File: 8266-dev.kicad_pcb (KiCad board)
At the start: 2 copper layers, 1 part, among them U1 ESP8266-12F_ESP-12F

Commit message: updated to v1
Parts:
- added BT1: Battery, Battery:BatteryHolder_MPD_BC2003_1x2032, F.Cu at (-32.3, 35.3)
- added C1: 10uF, Capacitor_SMD:C_1206_3216Metric, F.Cu at (-20.6, -21.4)
- added C2: 100nF, Capacitor_SMD:C_1206_3216Metric, F.Cu at (-15.3, -21.3)
- added G*** (x6): LOGO, LOGO, F.Cu at (0.00, 0.00)
- added J1: Conn_01x05_Female, digikey-kicad-library:PinHeader_1x5_P2.5mm_Drill1.1mm, F.Cu at (32.0, 35.0)
- added J2: Conn_01x05_Female, digikey-kicad-library:PinHeader_1x5_P2.5mm_Drill1.1mm, F.Cu at (-38.1, -34.8)
- added J3: Conn_01x06_Female, Connector_PinHeader_2.54mm:PinHeader_1x06_P2.54mm_Vertical, F.Cu at (19.8, 35.1)
- added J4: Conn_01x03_Female, digikey-kicad-library:PinHeader_1x3_P2.54_Drill1.1mm, F.Cu at (41.4, -32.7)
- added R1: 10K, Resistor_SMD:R_1206_3216Metric, F.Cu at (-19.9, -36.6)
- added R2: 10K, Resistor_SMD:R_1206_3216Metric, F.Cu at (-20.0, -32.7)
- added R3: 10K, Resistor_SMD:R_1206_3216Metric, F.Cu at (28.4, -40.5)
- added R4: 10K, Resistor_SMD:R_1206_3216Metric, F.Cu at (17.8, -24.4)
- added S1: 430152070826, digikey-kicad-library:Switch_Tactile_SMD_6x6mm, F.Cu at (31.3, -28.6)
- U1: moved to F.Cu
- moved U1 177.7 mm to (-0.53, -29.7), turned to 0 degrees
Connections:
- U1 pad 10: Net-(U1-Pad10) -> /MISO
- U1 pad 11: Net-(U1-Pad11) -> /IO9
- U1 pad 12: Net-(U1-Pad12) -> /IO10
- U1 pad 13: Net-(U1-Pad13) -> /MOSI
- U1 pad 14: Net-(U1-Pad14) -> /SCLK
- U1 pad 15: Net-(U1-Pad15) -> GND
- U1 pad 17: Net-(U1-Pad17) -> /IO2
- U1 pad 19: Net-(U1-Pad19) -> /IO4
- U1 pad 2: Net-(U1-Pad2) -> /ADC
- U1 pad 20: Net-(U1-Pad20) -> /IO5
- U1 pad 21: Net-(U1-Pad21) -> /rx
- U1 pad 22: Net-(U1-Pad22) -> /tx
- U1 pad 4: Net-(U1-Pad4) -> /IO16
- U1 pad 5: Net-(U1-Pad5) -> /IO14
- U1 pad 6: Net-(U1-Pad6) -> /IO12
- U1 pad 7: Net-(U1-Pad7) -> /IO13
- U1 pad 8: Net-(U1-Pad8) -> /VCC
- U1 pad 9: Net-(U1-Pad9) -> /CS0
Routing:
- net /rx: track 0.00 -> 93.3 mm, vias 0 -> 1
- net /tx: track 0.00 -> 92.5 mm, vias 0 -> 1
- net /SCLK: track 0.00 -> 62.7 mm
- net /MOSI: track 0.00 -> 62.5 mm
- net /IO10: track 0.00 -> 62.3 mm
- net /IO9: track 0.00 -> 62.1 mm
- net /MISO: track 0.00 -> 61.8 mm
- net /CS0: track 0.00 -> 61.7 mm
- net /IO2: track 0.00 -> 34.8 mm
- net /IO4: track 0.00 -> 34.7 mm, vias 0 -> 2
- net /IO5: track 0.00 -> 34.5 mm, vias 0 -> 2
- net /IO16: track 0.00 -> 30.7 mm
- net /IO14: track 0.00 -> 30.5 mm
- net /IO12: track 0.00 -> 30.3 mm
- net /ADC: track 0.00 -> 30.3 mm
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- added copper zone on B.Cu, net /VCC
- added copper zone on F.Cu, net GND
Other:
- net class Default: via_dia 0.8 -> 0.6
- rule pad_to_mask_clearance: 0.051 -> 0.2
- board text added: "ADC"
- board text added: "CS0"
- board text added: "GND"
- board text added: "IO10"
- board text added: "IO12"
- board text added: "IO13"
- board text added: "IO14"
- board text added: "IO16"
- board text added: "IO2"
- board text added: "IO4"
- board text added: "IO5"
- board text added: "IO9"
- board text added: "MISO"
- board text added: "MOSI"
- board text added: "RX"
- board text added: "SCLK"
- board text added: "TX"
- board text added: "VCC"
- board text added: "jack in here"
- board text added: "jigglebilly's ESP8266-12F dev v1.0"

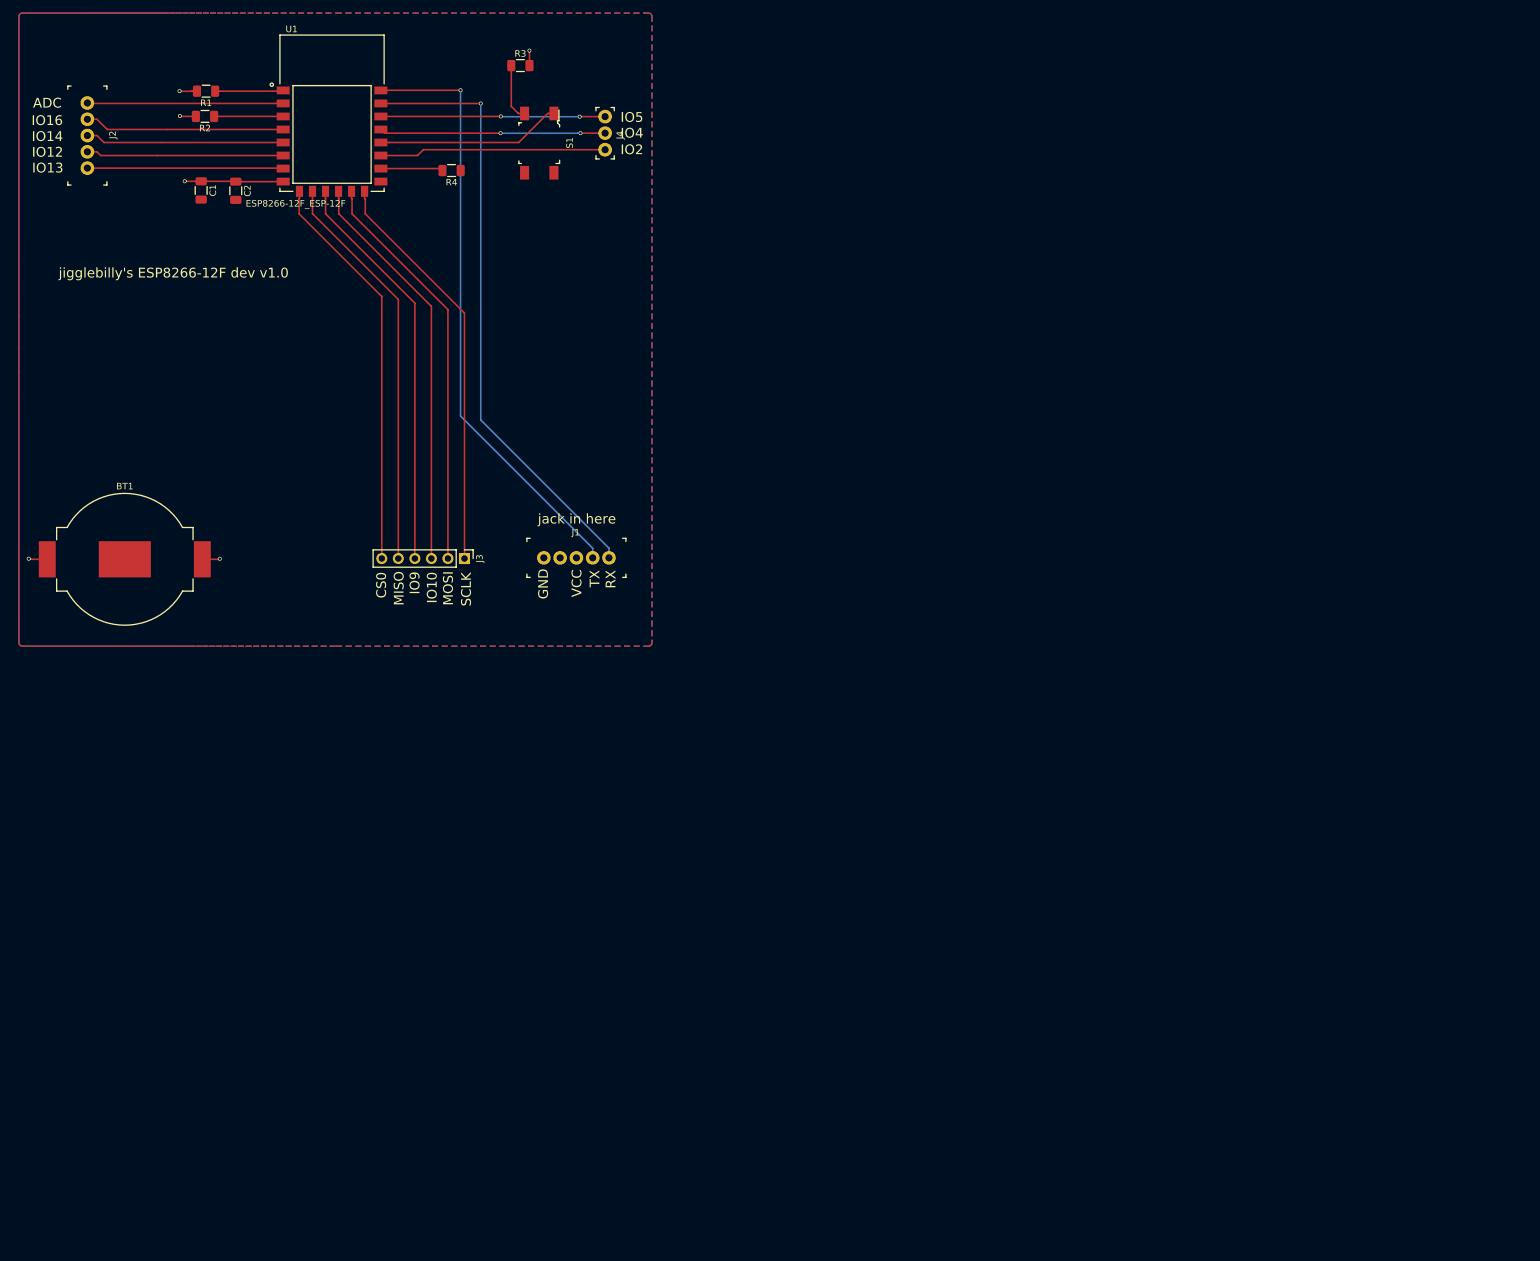
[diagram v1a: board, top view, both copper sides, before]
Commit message: added logic level shifter and some WS2812B's
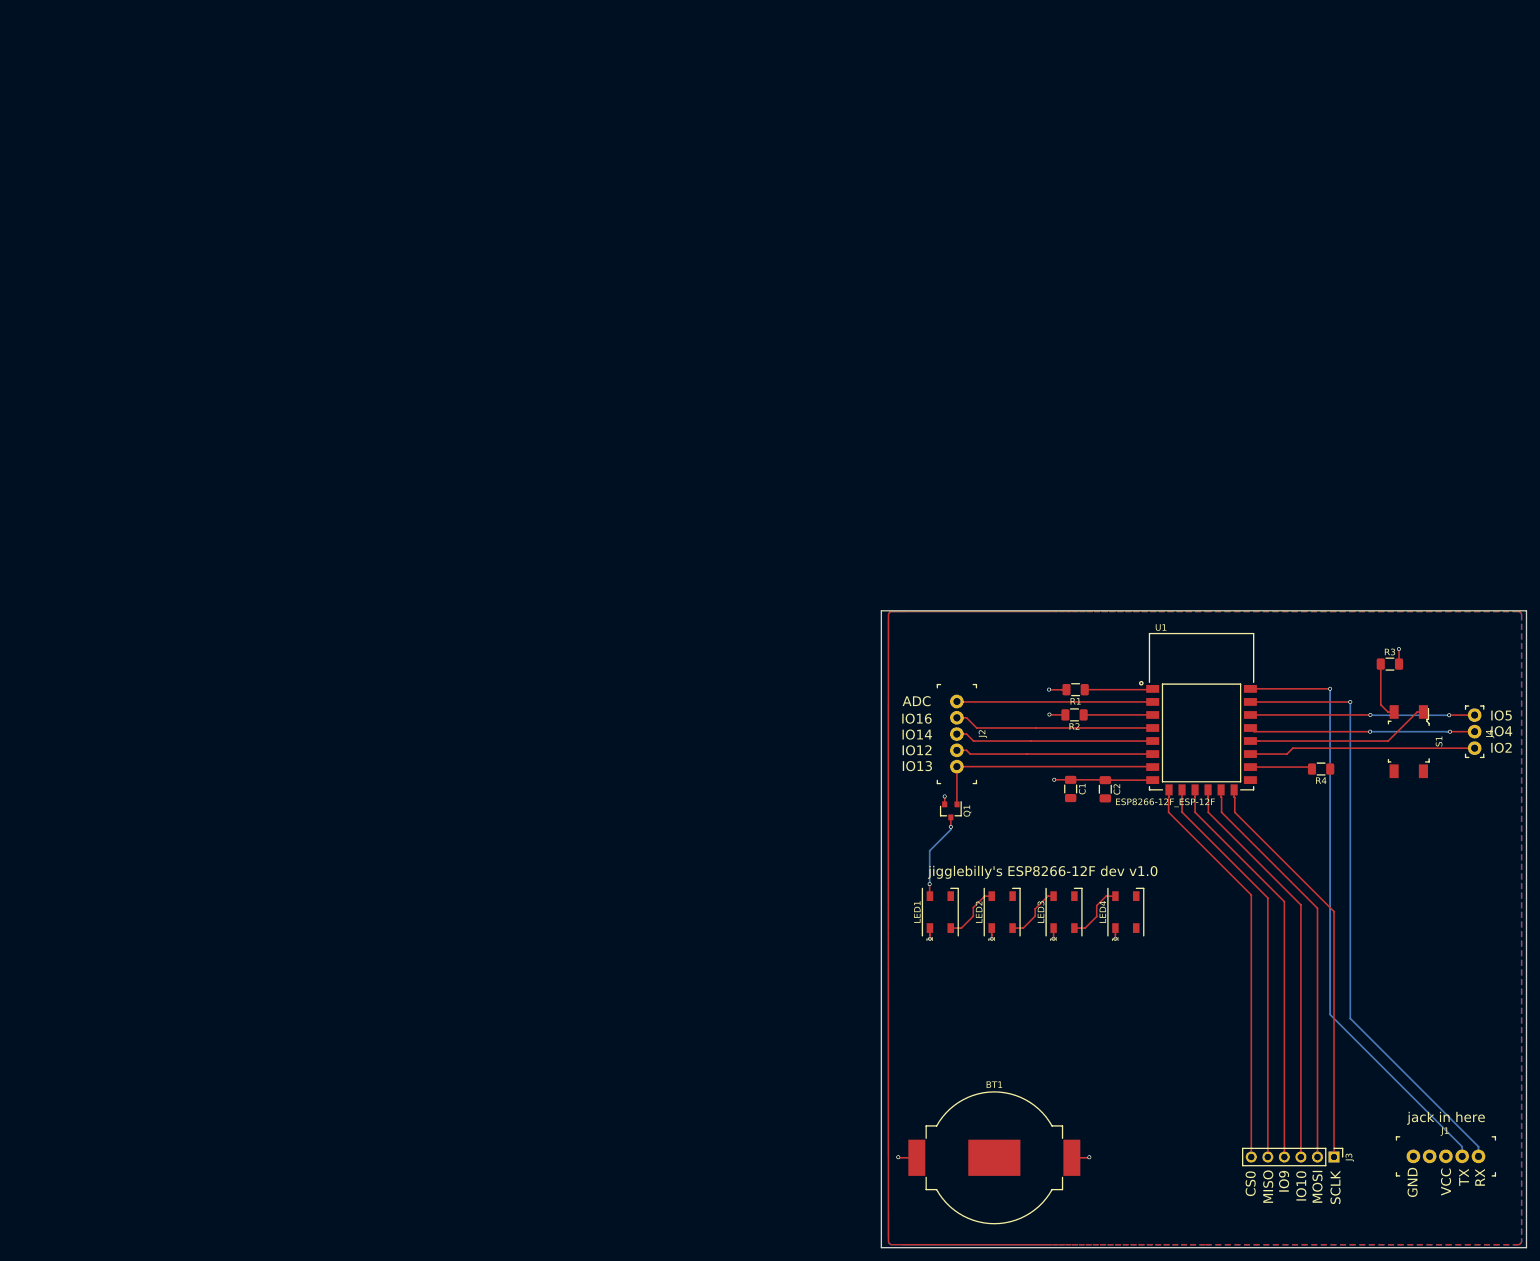
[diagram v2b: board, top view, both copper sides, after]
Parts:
- removed the G*** at (0.00, 0.00) (x6)
- added G*** (x6): LOGO, LOGO, F.Cu at (0.00, 0.00)
- added LED1: WS2812B, LED_SMD:LED_WS2812B_PLCC4_5.0x5.0mm_P3.2mm, F.Cu at (92.9, 89.4)
- added LED2: WS2812B, LED_SMD:LED_WS2812B_PLCC4_5.0x5.0mm_P3.2mm, F.Cu at (102.4, 89.4)
- added LED3: WS2812B, LED_SMD:LED_WS2812B_PLCC4_5.0x5.0mm_P3.2mm, F.Cu at (111.9, 89.4)
- added LED4: WS2812B, LED_SMD:LED_WS2812B_PLCC4_5.0x5.0mm_P3.2mm, F.Cu at (121.4, 89.4)
- added Q1: BSS138, Package_TO_SOT_SMD:SOT-23, F.Cu at (94.5, 73.9)
- moved BT1 162.1 mm to (101.2, 127.2)
- moved C1 162.1 mm to (112.9, 70.5)
- moved C2 162.1 mm to (118.2, 70.6)
- moved J1 162.1 mm to (165.5, 126.9)
- moved J2 162.1 mm to (95.4, 57.1)
- moved J3 162.1 mm to (153.3, 127.1)
- moved R1 162.1 mm to (113.6, 55.3)
- moved R2 162.1 mm to (113.5, 59.2)
- moved R3 162.1 mm to (161.9, 51.4)
- moved R4 162.1 mm to (151.3, 67.5)
- moved S1 162.1 mm to (164.8, 63.3)
- moved U1 162.1 mm to (133.0, 62.2)
- moved J4 162.1 mm to (174.9, 59.2)
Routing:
- net Net-(LED1-Pad4): track 0.00 -> 13.5 mm, vias 0 -> 2
- net Net-(LED3-Pad2): track 0.00 -> 9.30 mm
- net Net-(LED1-Pad2): track 0.00 -> 9.10 mm
- net Net-(LED2-Pad2): track 0.00 -> 8.98 mm
- net /VCC: track 28.3 -> 36.1 mm, vias 6 -> 11
- net /IO13: track 30.3 -> 36.1 mm
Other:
- board outline added: 99.1 x 97.8 mm

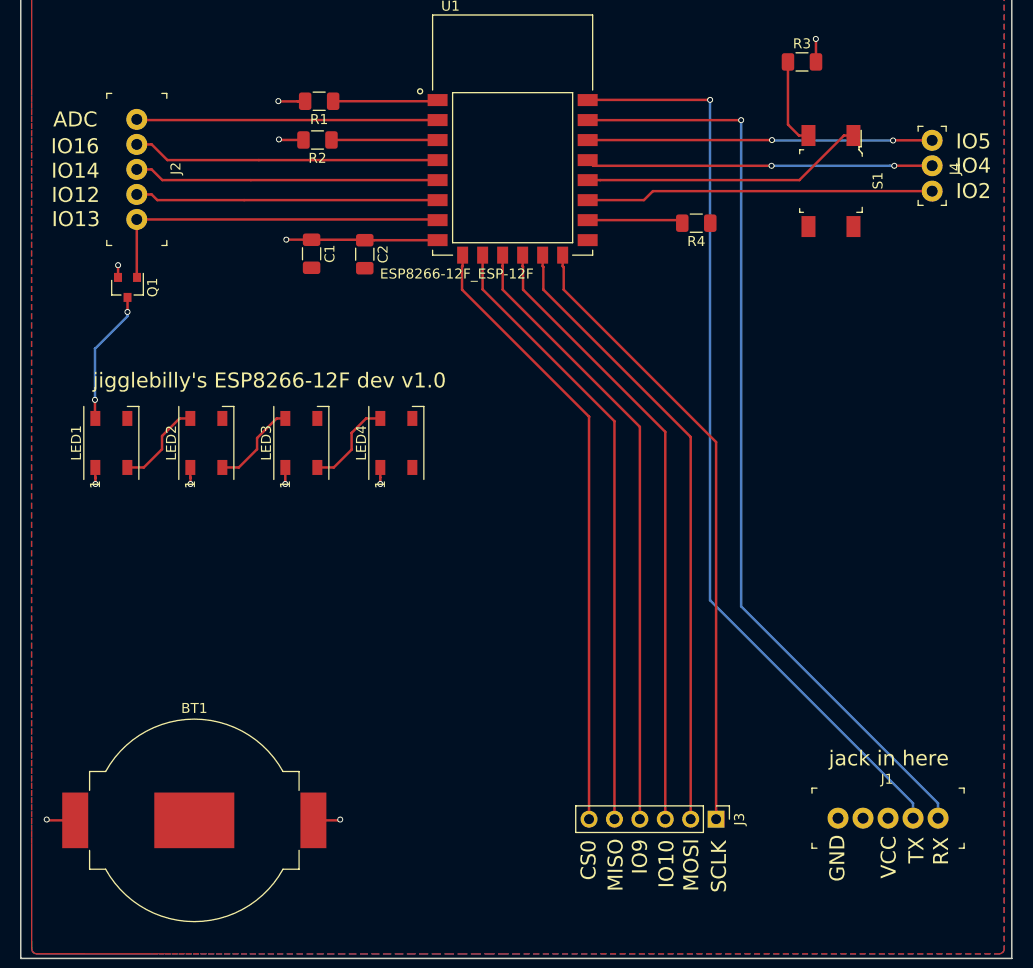
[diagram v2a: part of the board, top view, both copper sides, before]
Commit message: added power light, CH330N, and some neopixels
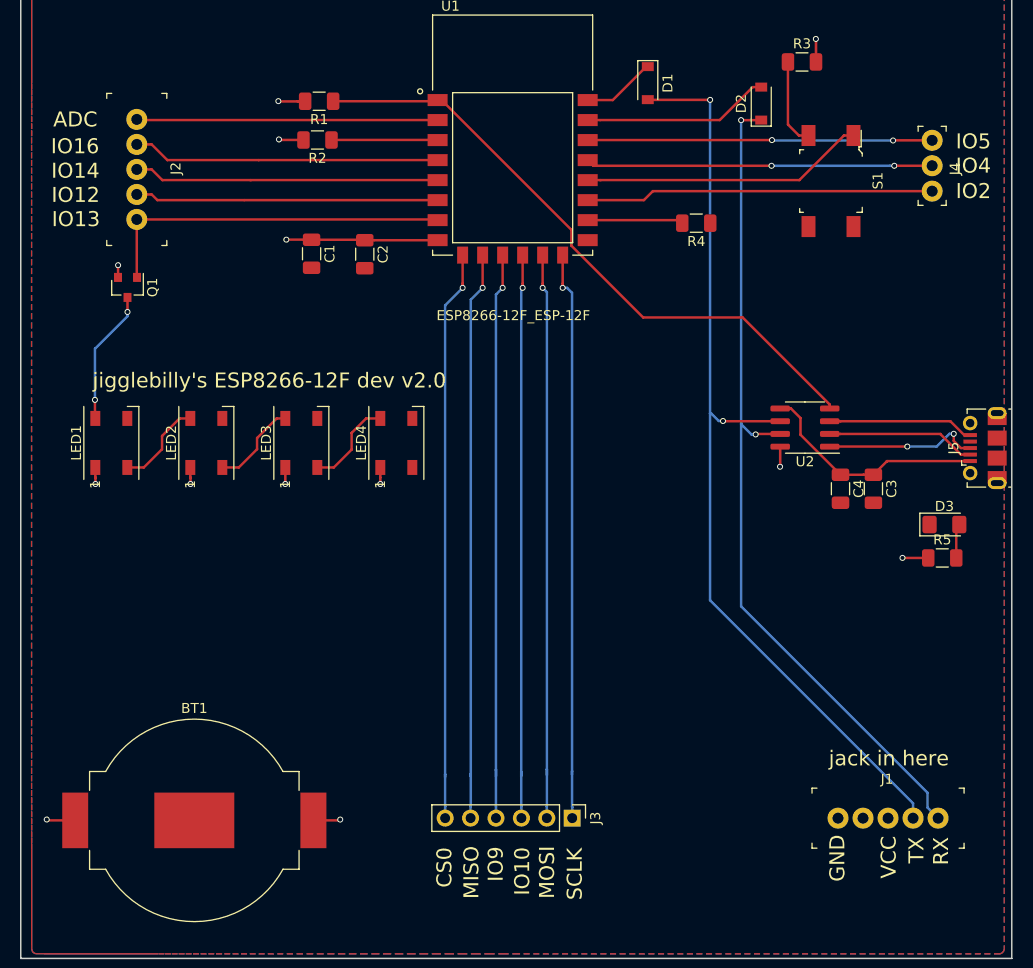
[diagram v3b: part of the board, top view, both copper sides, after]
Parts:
- removed the G*** at (0.00, 0.00) (x6)
- added C3: 100nF, Capacitor_SMD:C_1206_3216Metric, F.Cu at (169.0, 94.0)
- added C4: 100nF, Capacitor_SMD:C_1206_3216Metric, F.Cu at (165.8, 94.0)
- added D1: MBR0520, Diode_SMD:D_SOD-123, F.Cu at (146.5, 53.5)
- added D2: MBR0520, Diode_SMD:D_SOD-123, F.Cu at (157.8, 55.5)
- added D3: LED, LED_SMD:LED_1206_3216Metric_Pad1.42x1.75mm_HandSolder, F.Cu at (176.1, 97.6)
- added G*** (x6): LOGO, LOGO, F.Cu at (0.00, 0.00)
- added J5: USB_B_Micro, Connector_USB:USB_Micro-B_Molex-105017-0001, F.Cu at (180.2, 90.0)
- added R5: R, Resistor_SMD:R_1206_3216Metric, F.Cu at (175.9, 100.9)
- added U2: CH330N, Package_SO:SOIC-8_3.9x4.9mm_P1.27mm, F.Cu at (162.2, 87.9)
- moved J3 14.4 mm to (138.9, 126.9)
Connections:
- U1 pad 21: /rx -> Net-(D2-Pad2)
- U1 pad 22: /tx -> Net-(D1-Pad1)
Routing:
- net Net-(R1-Pad1): track 10.5 -> 63.6 mm
- net Net-(C3-Pad1): track 0.00 -> 23.3 mm
- net Net-(D2-Pad2): track 0.00 -> 18.7 mm
- net Net-(J5-Pad3): track 0.00 -> 15.6 mm, vias 0 -> 2
- net Net-(J5-Pad2): track 0.00 -> 14.9 mm
- net GND: track 0.00 -> 14.6 mm
- net /rx: track 93.3 -> 84.3 mm, vias 1 -> 2
- net Net-(D1-Pad1): track 0.00 -> 7.42 mm
- net /IO10: track 62.3 -> 56.8 mm, vias 0 -> 1
- net /MOSI: track 62.5 -> 57.0 mm, vias 0 -> 1
- net /SCLK: track 62.7 -> 57.3 mm, vias 0 -> 1
- net /IO9: track 62.1 -> 57.2 mm, vias 0 -> 1
- net /MISO: track 61.8 -> 57.1 mm, vias 0 -> 1
- net /VCC: track 36.1 -> 40.7 mm, vias 11 -> 13
- net /CS0: track 61.7 -> 57.3 mm, vias 0 -> 1
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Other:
- board text added: "jigglebilly's ESP8266-12F dev v2.0"
- board text removed: "jigglebilly's ESP8266-12F dev v1.0"

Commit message: update
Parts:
- removed D1, D2: MBR0520, Diode_SMD:D_SOD-123
- removed the G*** at (0.00, 0.00) (x6)
- added C5: 100nF, Capacitor_SMD:C_1206_3216Metric, F.Cu at (158.2, 93.6)
- added G*** (x6): LOGO, LOGO, F.Cu at (0.00, 0.00)
- D3: value LED -> GREEN LED
- J1: value Conn_01x05_Female -> Programming headers
- J2: value Conn_01x05_Female -> Left breakout
- J3: value Conn_01x06_Female -> Bottom breakout
- J4: value Conn_01x03_Female -> Right breakout
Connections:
- net Net-(C3-Pad1) renamed /VBUS
- net Net-(J5-Pad2) renamed /D-
- net Net-(J5-Pad3) renamed /D+
- net Net-(R1-Pad1) renamed /RTS
- J5 pad 6: Net-(J5-Pad6) -> GND
- U1 pad 21: Net-(D2-Pad2) -> /tx
- U1 pad 22: Net-(D1-Pad1) -> /rx
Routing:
- net Net-(D2-Pad2): track 18.7 -> 0.00 mm
- net /rx: track 84.3 -> 96.6 mm
- net Net-(D1-Pad1): track 7.42 -> 0.00 mm
- net /VCC: track 40.7 -> 46.0 mm
- net /tx: track 93.8 -> 96.5 mm
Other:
- board text added: "jigglebilly's ESP8266-12F dev v2.1 This better fucking work!"
- board text removed: "jigglebilly's ESP8266-12F dev v2.0"
